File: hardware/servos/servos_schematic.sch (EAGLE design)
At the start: 10 parts, among them IC1 7805T

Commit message: Updating schematics of servos and ledarrows to include the db15 connector used to interface outside of the electronics enclosure.
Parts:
- removed JP3, JP4: (no value), adafruit:PINHD-1X1
- added X1: (no value), adafruit:F15H
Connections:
- net 5V: now also X1.13
- net GROUND: now also X1.14
- net N$6: now also X1.5; no longer JP3.1
- net N$7: now also X1.6; no longer JP4.1
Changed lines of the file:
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@@
 <part name="R1" library="resistor" deviceset="R-US_" device="0204/5"/>
 <part name="R2" library="resistor" deviceset="R-US_" device="0204/5"/>
-<part name="JP3" library="adafruit" deviceset="PINHD-1X1" device=""/>
-<part name="JP4" library="adafruit" deviceset="PINHD-1X1" device=""/>
 <part name="JP5" library="pinhead" deviceset="PINHD-1X2" device=""/>
 <part name="IC1" library="adafruit" deviceset="78*" device="T" technology="05"/>
 <part name="C1" library="adafruit" deviceset="C-US" device="025-050X050"/>
 <part name="C2" library="adafruit" deviceset="C-US" device="025-050X050"/>
+<part name="X1" library="adafruit" deviceset="F15" device="H"/>
 </parts>
 <sheets>
@@
 <instance part="R1" gate="G$1" x="60.96" y="81.28" rot="R90"/>
 <instance part="R2" gate="G$1" x="73.66" y="81.28" rot="R90"/>
-<instance part="JP3" gate="G$1" x="66.04" y="68.58"/>
-<instance part="JP4" gate="G$1" x="86.36" y="68.58"/>
 <instance part="JP5" gate="G$1" x="-33.02" y="86.36"/>
 <instance part="IC1" gate="A1" x="-5.08" y="88.9"/>
 <instance part="C1" gate="G$1" x="-17.78" y="81.28"/>
 <instance part="C2" gate="G$1" x="10.16" y="81.28"/>
+<instance part="X1" gate="-1" x="86.36" y="63.5"/>
 </instances>
 <busses>
@@
 <wire x1="-35.56" y1="86.36" x2="-27.94" y2="86.36" width="0.1524" layer="91"/>
 <wire x1="-27.94" y1="86.36" x2="-27.94" y2="73.66" width="0.1524" layer="91"/>
+<wire x1="55.88" y1="43.18" x2="99.06" y2="43.18" width="0.1524" layer="91"/>
+<junction x="55.88" y="43.18"/>
+<junction x="10.16" y="73.66"/>
+<wire x1="99.06" y1="43.18" x2="99.06" y2="58.42" width="0.1524" layer="91"/>
+<pinref part="X1" gate="-1" pin="14"/>
+<wire x1="99.06" y1="58.42" x2="93.98" y2="58.42" width="0.1524" layer="91"/>
 </segment>
 </net>
@@
 <junction x="10.16" y="88.9"/>
 <junction x="60.96" y="88.9"/>
+<wire x1="73.66" y1="88.9" x2="99.06" y2="88.9" width="0.1524" layer="91"/>
+<junction x="73.66" y="88.9"/>
+<pinref part="X1" gate="-1" pin="13"/>
+<wire x1="93.98" y1="60.96" x2="99.06" y2="60.96" width="0.1524" layer="91"/>
+<wire x1="99.06" y1="60.96" x2="99.06" y2="88.9" width="0.1524" layer="91"/>
 </segment>
 </net>
@@
 <pinref part="OK1" gate="A" pin="COL"/>
 <wire x1="60.96" y1="76.2" x2="53.34" y2="76.2" width="0.1524" layer="91"/>
-<wire x1="60.96" y1="76.2" x2="63.5" y2="76.2" width="0.1524" layer="91"/>
-<pinref part="JP3" gate="G$1" pin="1"/>
-<wire x1="63.5" y1="76.2" x2="63.5" y2="68.58" width="0.1524" layer="91"/>
 <junction x="60.96" y="76.2"/>
+<wire x1="60.96" y1="76.2" x2="68.58" y2="76.2" width="0.1524" layer="91"/>
+<wire x1="68.58" y1="76.2" x2="68.58" y2="60.96" width="0.1524" layer="91"/>
+<pinref part="X1" gate="-1" pin="5"/>
+<wire x1="68.58" y1="60.96" x2="78.74" y2="60.96" width="0.1524" layer="91"/>
 </segment>
 </net>
@@
 <segment>
 <pinref part="R2" gate="G$1" pin="1"/>
-<wire x1="73.66" y1="76.2" x2="73.66" y2="68.58" width="0.1524" layer="91"/>
+<wire x1="73.66" y1="76.2" x2="73.66" y2="58.42" width="0.1524" layer="91"/>
 <pinref part="OK1" gate="B" pin="COL"/>
-<wire x1="73.66" y1="68.58" x2="73.66" y2="58.42" width="0.1524" layer="91"/>
 <wire x1="73.66" y1="58.42" x2="53.34" y2="58.42" width="0.1524" layer="91"/>
-<pinref part="JP4" gate="G$1" pin="1"/>
-<wire x1="73.66" y1="68.58" x2="83.82" y2="68.58" width="0.1524" layer="91"/>
-<junction x="73.66" y="68.58"/>
+<wire x1="73.66" y1="58.42" x2="78.74" y2="58.42" width="0.1524" layer="91"/>
+<junction x="73.66" y="58.42"/>
+<pinref part="X1" gate="-1" pin="6"/>
 </segment>
 </net>

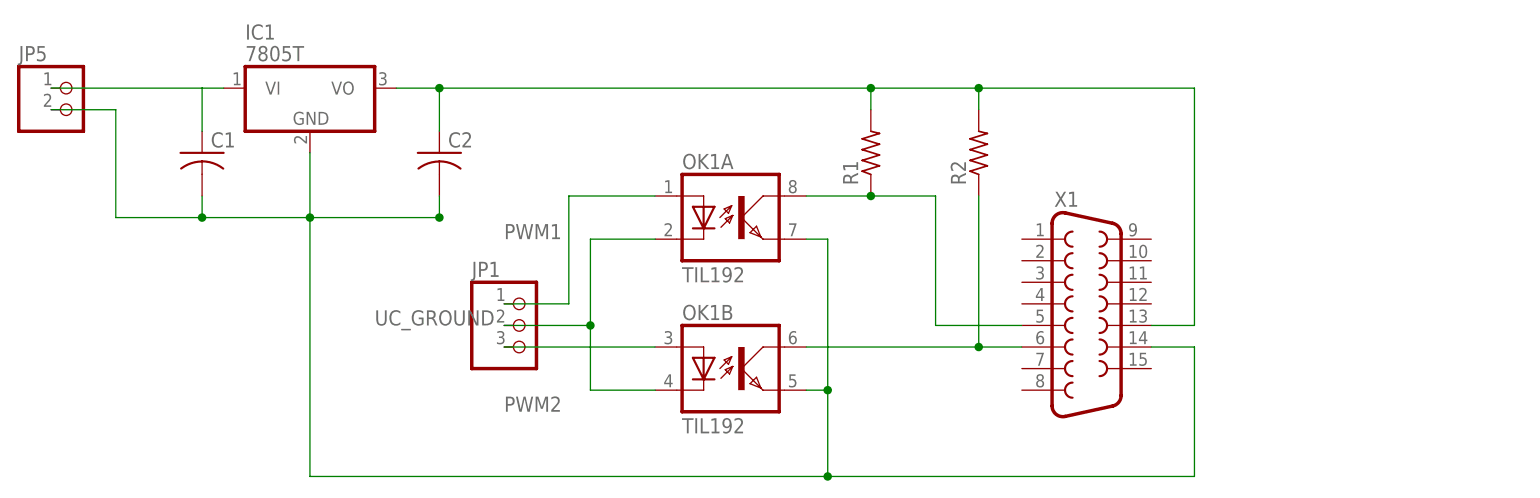
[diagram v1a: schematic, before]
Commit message: Schematics updates: Adding a shield schematic file for the microcontroller board header connector and power breakdown. Adding page border to existing schematics. Adding a few component values. Updating the display schematic to use common cathode 7 segment.
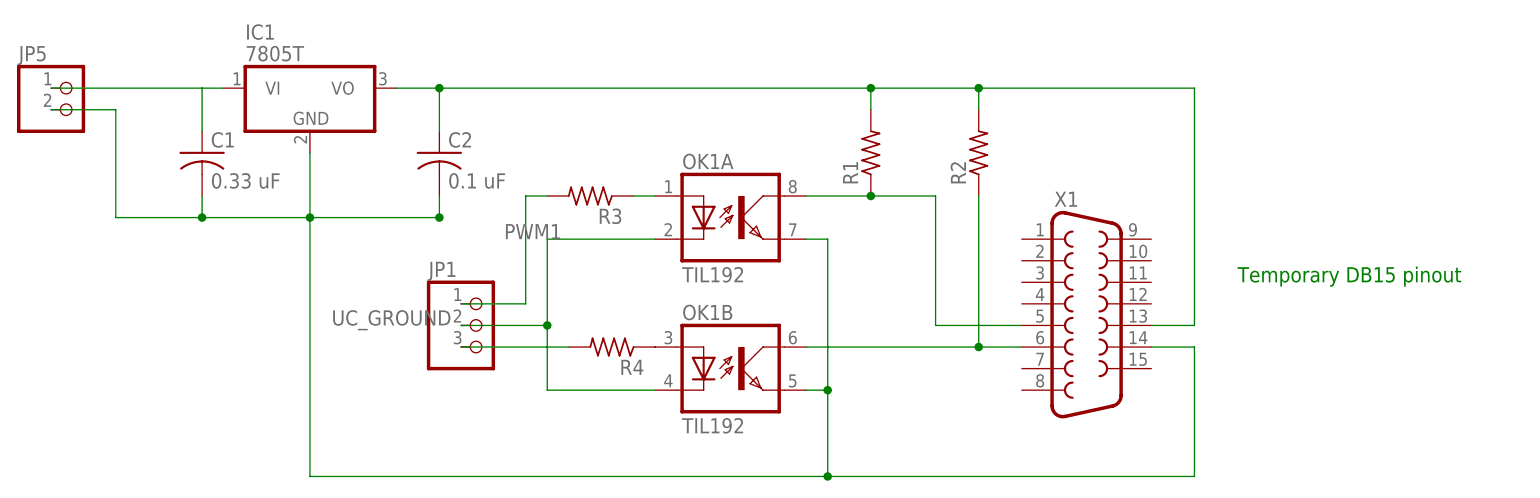
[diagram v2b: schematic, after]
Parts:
- added R3, R4: (no value), resistor:R-US_0204/5
- C1: value (none) -> 0.33 uF
- C2: value (none) -> 0.1 uF
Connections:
- removed net PWM2: JP1.3, OK1B.A
- new net N$1: OK1A.A, R3.1
- new net N$2: OK1B.A, R4.1
- new net N$3: JP1.3, R4.2
- net PWM1: now also R3.2; no longer OK1A.A
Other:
- note added: "Temporary DB15 pinout"
- moved on the sheet: JP1
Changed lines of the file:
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@@
 <part name="JP5" library="pinhead" deviceset="PINHD-1X2" device=""/>
 <part name="IC1" library="adafruit" deviceset="78*" device="T" technology="05"/>
-<part name="C1" library="adafruit" deviceset="C-US" device="025-050X050"/>
-<part name="C2" library="adafruit" deviceset="C-US" device="025-050X050"/>
+<part name="C1" library="adafruit" deviceset="C-US" device="025-050X050" value="0.33 uF"/>
+<part name="C2" library="adafruit" deviceset="C-US" device="025-050X050" value="0.1 uF"/>
 <part name="X1" library="adafruit" deviceset="F15" device="H"/>
+<part name="FRAME1" library="frames" deviceset="DINA4_L" device=""/>
+<part name="R3" library="resistor" deviceset="R-US_" device="0204/5"/>
+<part name="R4" library="resistor" deviceset="R-US_" device="0204/5"/>
 </parts>
 <sheets>
 <sheet>
 <plain>
+<text x="104.14" y="66.04" size="1.778" layer="91">Temporary DB15 pinout</text>
 </plain>
 <instances>
 <instance part="OK1" gate="A" x="45.72" y="73.66"/>
 <instance part="OK1" gate="B" x="45.72" y="55.88"/>
-<instance part="JP1" gate="A" x="20.32" y="60.96"/>
+<instance part="JP1" gate="A" x="15.24" y="60.96"/>
 <instance part="R1" gate="G$1" x="60.96" y="81.28" rot="R90"/>
 <instance part="R2" gate="G$1" x="73.66" y="81.28" rot="R90"/>
@@
 <instance part="C2" gate="G$1" x="10.16" y="81.28"/>
 <instance part="X1" gate="-1" x="86.36" y="63.5"/>
+<instance part="FRAME1" gate="G$1" x="-91.44" y="-22.86"/>
+<instance part="FRAME1" gate="G$2" x="71.12" y="-22.86" smashed="yes">
+<attribute name="LAST_DATE_TIME" x="83.82" y="-21.59" size="2.54" layer="94" font="vector"/>
+<attribute name="SHEET" x="157.48" y="-21.59" size="2.54" layer="94" font="vector"/>
+<attribute name="DRAWING_NAME" x="88.9" y="-3.81" size="2.54" layer="94" font="vector"/>
+</instance>
+<instance part="R3" gate="G$1" x="27.94" y="76.2" rot="R180"/>
+<instance part="R4" gate="G$1" x="30.48" y="58.42" rot="R180"/>
 </instances>
 <busses>
@@
 <net name="UC_GROUND" class="0">
 <segment>
-<wire x1="17.78" y1="60.96" x2="27.94" y2="60.96" width="0.1524" layer="91"/>
-<wire x1="27.94" y1="60.96" x2="27.94" y2="53.34" width="0.1524" layer="91"/>
+<wire x1="12.7" y1="60.96" x2="22.86" y2="60.96" width="0.1524" layer="91"/>
+<wire x1="22.86" y1="60.96" x2="22.86" y2="53.34" width="0.1524" layer="91"/>
 <pinref part="OK1" gate="B" pin="C"/>
-<wire x1="27.94" y1="53.34" x2="35.56" y2="53.34" width="0.1524" layer="91"/>
+<wire x1="22.86" y1="53.34" x2="35.56" y2="53.34" width="0.1524" layer="91"/>
 <pinref part="OK1" gate="A" pin="C"/>
-<wire x1="35.56" y1="71.12" x2="27.94" y2="71.12" width="0.1524" layer="91"/>
-<wire x1="27.94" y1="71.12" x2="27.94" y2="60.96" width="0.1524" layer="91"/>
-<junction x="27.94" y="60.96"/>
+<wire x1="35.56" y1="71.12" x2="22.86" y2="71.12" width="0.1524" layer="91"/>
+<wire x1="22.86" y1="71.12" x2="22.86" y2="60.96" width="0.1524" layer="91"/>
+<junction x="22.86" y="60.96"/>
 <pinref part="JP1" gate="A" pin="2"/>
-<label x="2.54" y="60.96" size="1.778" layer="95"/>
-</segment>
-</net>
-<net name="PWM2" class="0">
-<segment>
-<wire x1="17.78" y1="58.42" x2="35.56" y2="58.42" width="0.1524" layer="91"/>
-<pinref part="OK1" gate="B" pin="A"/>
-<pinref part="JP1" gate="A" pin="3"/>
-<label x="17.78" y="50.8" size="1.778" layer="95"/>
+<label x="-2.54" y="60.96" size="1.778" layer="95"/>
 </segment>
 </net>
@@
 <segment>
 <pinref part="JP1" gate="A" pin="1"/>
-<wire x1="17.78" y1="63.5" x2="25.4" y2="63.5" width="0.1524" layer="91"/>
-<wire x1="25.4" y1="63.5" x2="25.4" y2="76.2" width="0.1524" layer="91"/>
-<pinref part="OK1" gate="A" pin="A"/>
-<wire x1="25.4" y1="76.2" x2="35.56" y2="76.2" width="0.1524" layer="91"/>
+<wire x1="12.7" y1="63.5" x2="20.32" y2="63.5" width="0.1524" layer="91"/>
 <label x="17.78" y="71.12" size="1.778" layer="95"/>
+<wire x1="20.32" y1="63.5" x2="20.32" y2="76.2" width="0.1524" layer="91"/>
+<pinref part="R3" gate="G$1" pin="2"/>
+<wire x1="22.86" y1="76.2" x2="20.32" y2="76.2" width="0.1524" layer="91"/>
 </segment>
 </net>
@@
 </segment>
 </net>
+<net name="N$1" class="0">
+<segment>
+<pinref part="OK1" gate="A" pin="A"/>
+<pinref part="R3" gate="G$1" pin="1"/>
+<wire x1="33.02" y1="76.2" x2="35.56" y2="76.2" width="0.1524" layer="91"/>
+</segment>
+</net>
+<net name="N$2" class="0">
+<segment>
+<pinref part="OK1" gate="B" pin="A"/>
+<pinref part="R4" gate="G$1" pin="1"/>
+</segment>
+</net>
+<net name="N$3" class="0">
+<segment>
+<pinref part="R4" gate="G$1" pin="2"/>
+<pinref part="JP1" gate="A" pin="3"/>
+<wire x1="25.4" y1="58.42" x2="12.7" y2="58.42" width="0.1524" layer="91"/>
+</segment>
+</net>

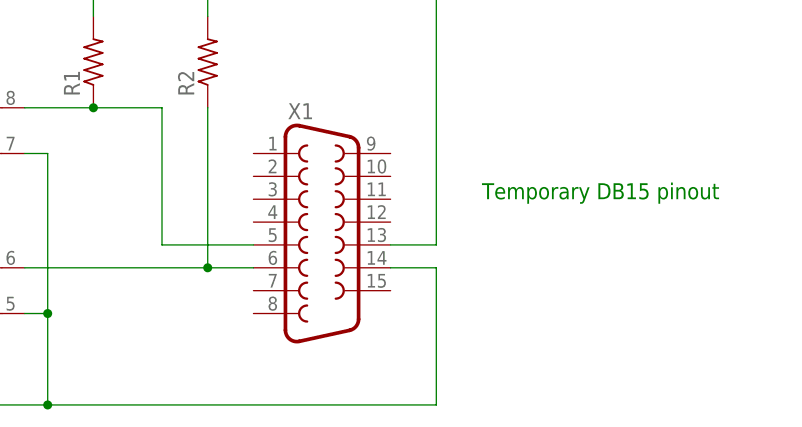
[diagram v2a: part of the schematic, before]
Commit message: Updating the schematics to include A5 frames and complete some component values. Also adding the arduino shield symbol to the shield schematic.
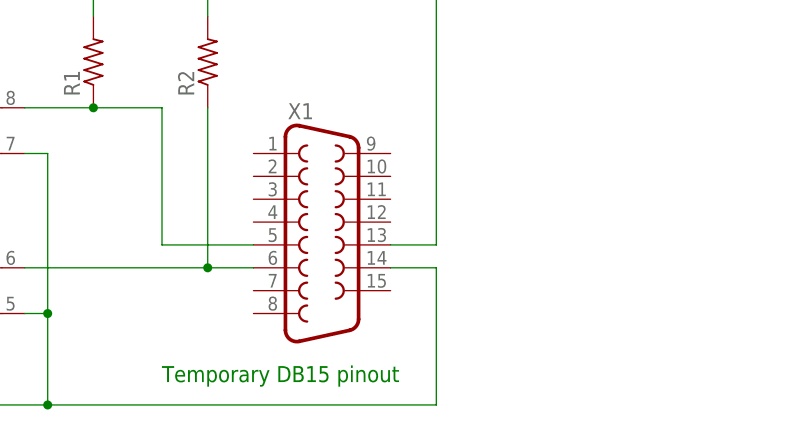
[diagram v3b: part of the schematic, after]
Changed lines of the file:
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@@
 <part name="C2" library="adafruit" deviceset="C-US" device="025-050X050" value="0.1 uF"/>
 <part name="X1" library="adafruit" deviceset="F15" device="H"/>
-<part name="FRAME1" library="frames" deviceset="DINA4_L" device=""/>
 <part name="R3" library="resistor" deviceset="R-US_" device="0204/5"/>
 <part name="R4" library="resistor" deviceset="R-US_" device="0204/5"/>
+<part name="FRAME2" library="frames" deviceset="DINA5_L" device=""/>
 </parts>
 <sheets>
 <sheet>
 <plain>
-<text x="104.14" y="66.04" size="1.778" layer="91">Temporary DB15 pinout</text>
+<text x="68.58" y="45.72" size="1.778" layer="91">Temporary DB15 pinout</text>
 </plain>
 <instances>
@@
 <instance part="C2" gate="G$1" x="10.16" y="81.28"/>
 <instance part="X1" gate="-1" x="86.36" y="63.5"/>
-<instance part="FRAME1" gate="G$1" x="-91.44" y="-22.86"/>
-<instance part="FRAME1" gate="G$2" x="71.12" y="-22.86" smashed="yes">
-<attribute name="LAST_DATE_TIME" x="83.82" y="-21.59" size="2.54" layer="94" font="vector"/>
-<attribute name="SHEET" x="157.48" y="-21.59" size="2.54" layer="94" font="vector"/>
-<attribute name="DRAWING_NAME" x="88.9" y="-3.81" size="2.54" layer="94" font="vector"/>
-</instance>
 <instance part="R3" gate="G$1" x="27.94" y="76.2" rot="R180"/>
 <instance part="R4" gate="G$1" x="30.48" y="58.42" rot="R180"/>
+<instance part="FRAME2" gate="G$1" x="-58.42" y="0"/>
 </instances>
 <busses>

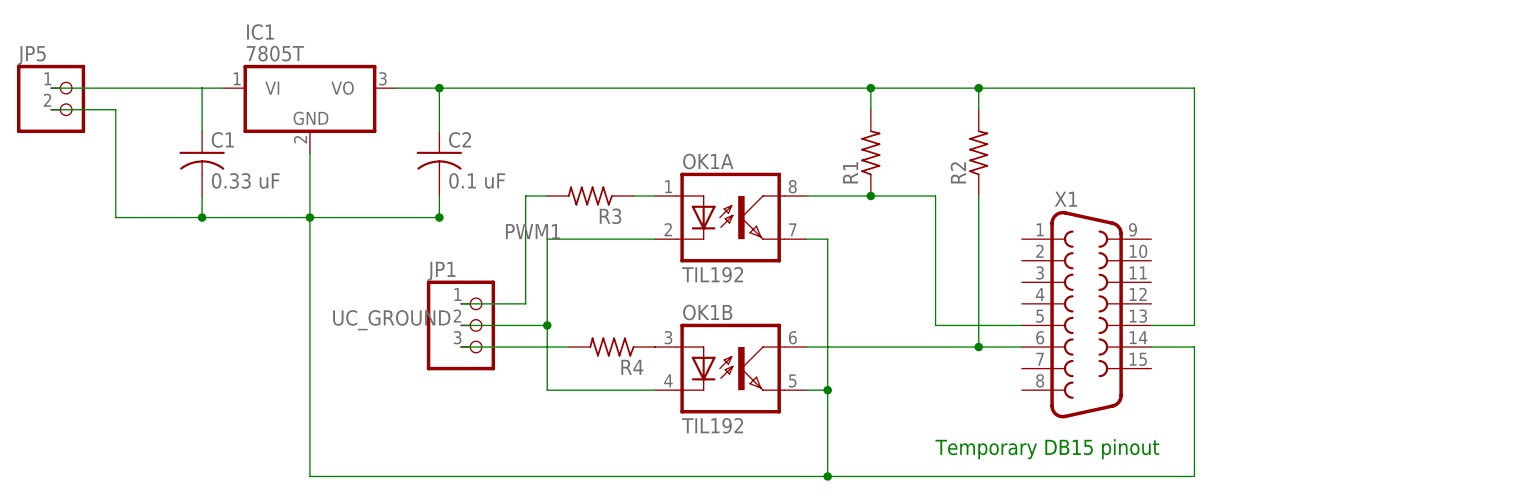
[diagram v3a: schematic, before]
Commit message: updating resistor values in schematics
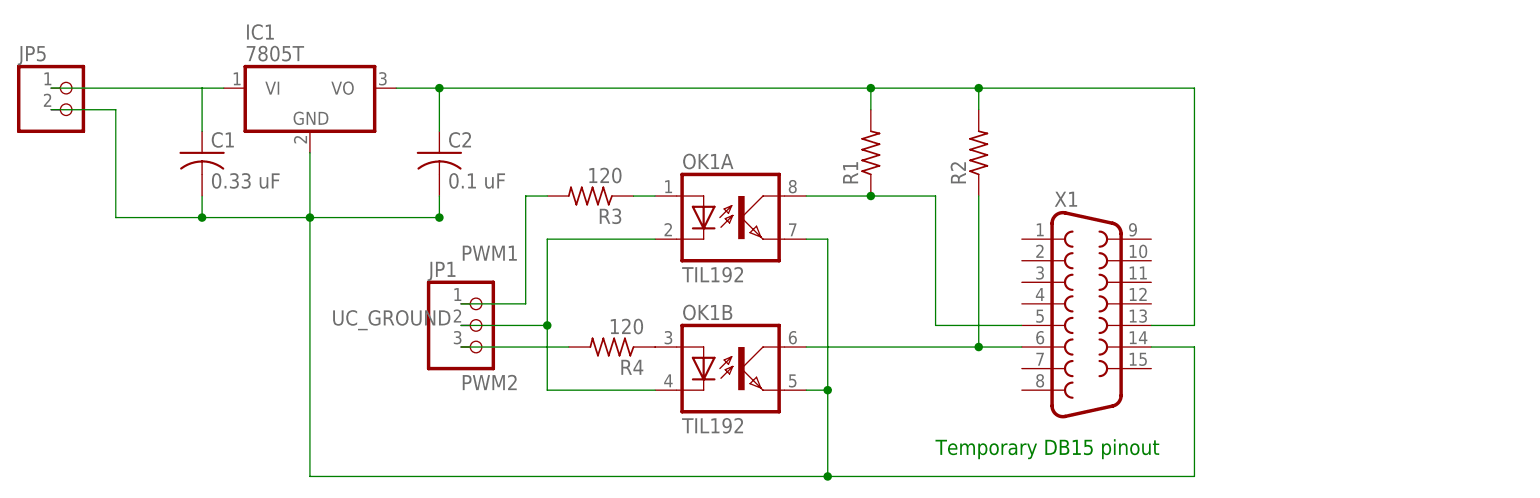
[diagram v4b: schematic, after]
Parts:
- R3, R4: value (none) -> 120
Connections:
- net N$3 renamed PWM2
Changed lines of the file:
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@@
 <part name="C2" library="adafruit" deviceset="C-US" device="025-050X050" value="0.1 uF"/>
 <part name="X1" library="adafruit" deviceset="F15" device="H"/>
-<part name="R3" library="resistor" deviceset="R-US_" device="0204/5"/>
-<part name="R4" library="resistor" deviceset="R-US_" device="0204/5"/>
+<part name="R3" library="resistor" deviceset="R-US_" device="0204/5" value="120"/>
+<part name="R4" library="resistor" deviceset="R-US_" device="0204/5" value="120"/>
 <part name="FRAME2" library="frames" deviceset="DINA5_L" device=""/>
 </parts>
@@
 <pinref part="JP1" gate="A" pin="1"/>
 <wire x1="12.7" y1="63.5" x2="20.32" y2="63.5" width="0.1524" layer="91"/>
-<label x="17.78" y="71.12" size="1.778" layer="95"/>
+<label x="12.7" y="68.58" size="1.778" layer="95"/>
 <wire x1="20.32" y1="63.5" x2="20.32" y2="76.2" width="0.1524" layer="91"/>
 <pinref part="R3" gate="G$1" pin="2"/>
@@
 </segment>
 </net>
-<net name="N$3" class="0">
+<net name="PWM2" class="0">
 <segment>
 <pinref part="R4" gate="G$1" pin="2"/>
 <pinref part="JP1" gate="A" pin="3"/>
 <wire x1="25.4" y1="58.42" x2="12.7" y2="58.42" width="0.1524" layer="91"/>
+<label x="12.7" y="53.34" size="1.778" layer="95"/>
 </segment>
 </net>
